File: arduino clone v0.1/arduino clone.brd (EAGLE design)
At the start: 77.5 x 27.6 mm, 47 parts, among them J203 ICSP HEADER, J402 FTDI Breakout Header, U101 ATMEGA328P_TQFP, U301 CH340G, Y101 16MHz, Y301 12MHz

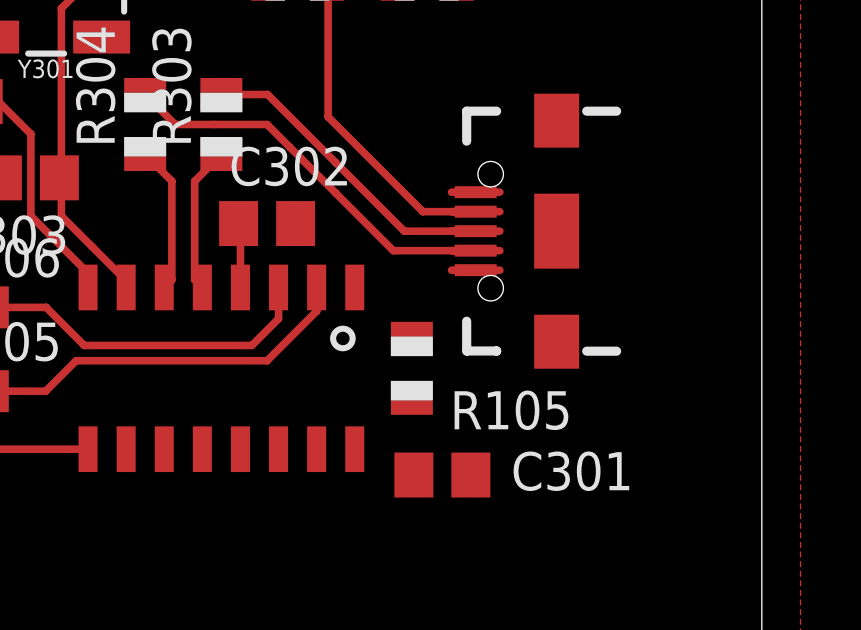
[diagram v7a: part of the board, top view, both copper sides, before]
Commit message: add shape for PP5V0_USB
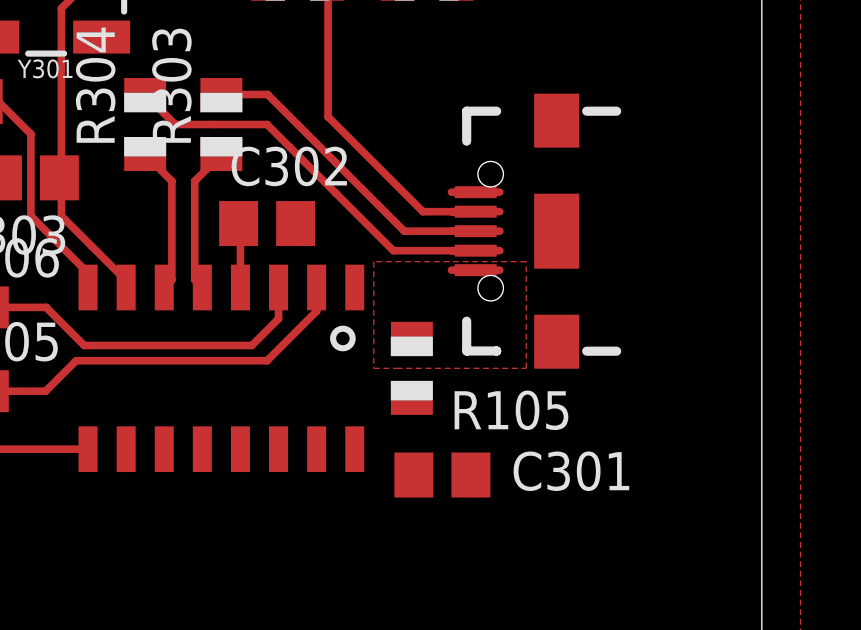
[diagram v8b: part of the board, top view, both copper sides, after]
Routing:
- added copper zone on layer 1, net PP5V0_USB
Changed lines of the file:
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@@
 <contactref element="J401" pad="VBUS1"/>
 <contactref element="J402" pad="3"/>
+<polygon width="0.0762" layer="1">
+<vertex x="74.168" y="47.498"/>
+<vertex x="78.486" y="47.498"/>
+<vertex x="78.486" y="51.054"/>
+<vertex x="73.406" y="51.054"/>
+<vertex x="73.406" y="47.498"/>
+</polygon>
 <wire x1="76.802" y1="50.77" x2="76.184" y2="60.452" width="0" layer="19" extent="1-1"/>
+<wire x1="74.676" y1="48.498" x2="76.802" y2="50.77" width="0" layer="19" extent="1-1"/>
 <wire x1="57.15" y1="63.5" x2="76.184" y2="60.452" width="0" layer="19" extent="1-1"/>
 <wire x1="50.546" y1="50.8" x2="57.15" y2="63.5" width="0" layer="19" extent="1-1"/>
@@
 <wire x1="12.7" y1="53.848" x2="24.13" y2="63.5" width="0" layer="19" extent="1-1"/>
 <wire x1="-11.7" y1="36.322" x2="12.7" y2="53.848" width="0" layer="19" extent="1-1"/>
-<wire x1="74.676" y1="48.498" x2="-11.7" y2="36.322" width="0" layer="19" extent="1-1"/>
 </signal>
 <signal name="PP5V0_CH340G">
@@
 <contactref element="C301" pad="1"/>
 <contactref element="R307" pad="2"/>
-<wire x1="74.742" y1="43.942" x2="72.771" y2="44.803" width="0" layer="19" extent="1-1"/>
+<wire x1="74.742" y1="43.942" x2="74.676" y2="46.498" width="0" layer="19" extent="1-1"/>
+<wire x1="72.771" y1="44.803" x2="74.742" y2="43.942" width="0" layer="19" extent="1-1"/>
 <wire x1="-18.05" y1="44.196" x2="72.771" y2="44.803" width="0" layer="19" extent="1-1"/>
-<wire x1="74.676" y1="46.498" x2="-18.05" y2="44.196" width="0" layer="19" extent="1-1"/>
 </signal>
 <signal name="MCU_D14">
